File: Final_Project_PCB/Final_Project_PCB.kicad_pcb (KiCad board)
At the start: 2 copper layers, 90 x 93 mm, 17 parts, among them J1 Screw_Terminal_01x03, J2 SR04 Sensor Jarak, J3 LDR, J4 Soil Moisture Sensor, K1 SRD-05VDC-SL-C, Q1 BC547, U1 ESP32-DEVKIT-V1, U2 DHT11

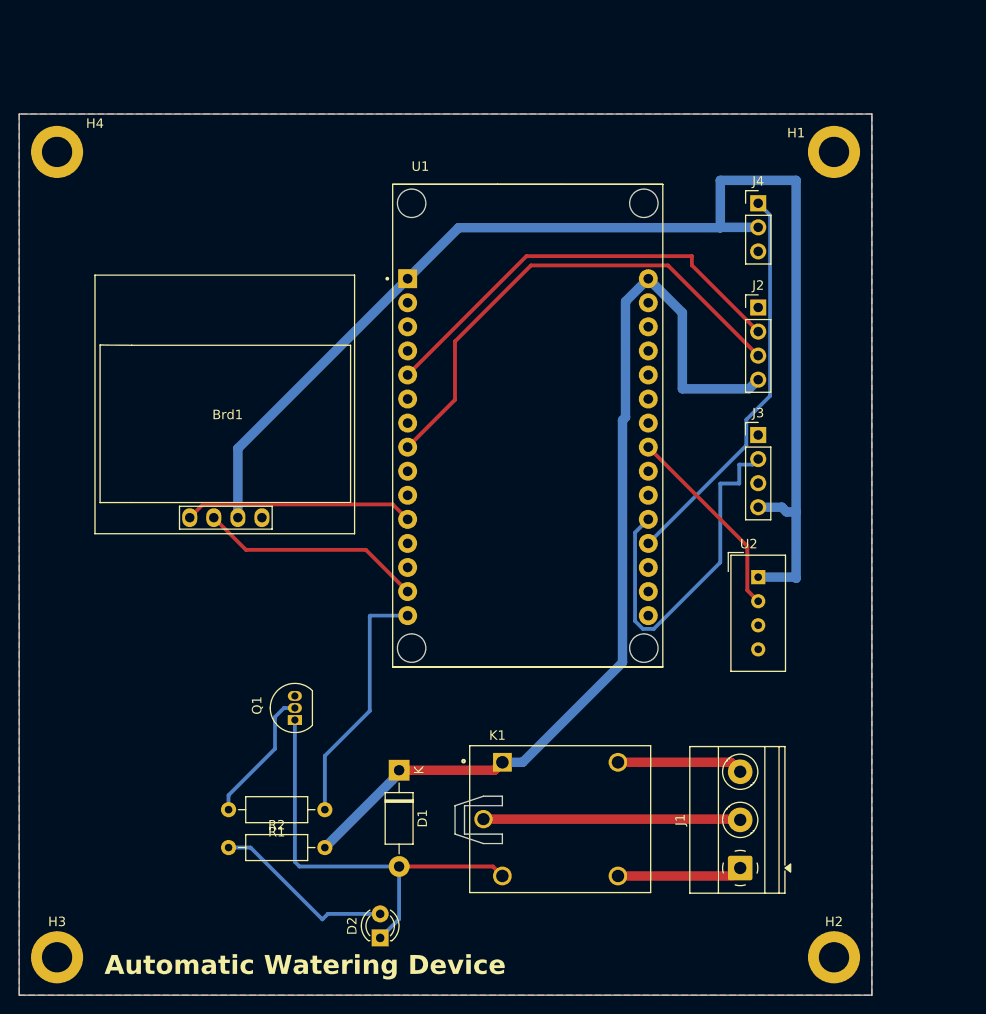
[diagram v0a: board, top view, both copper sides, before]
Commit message: Adding Barrel Jack for 5v Source
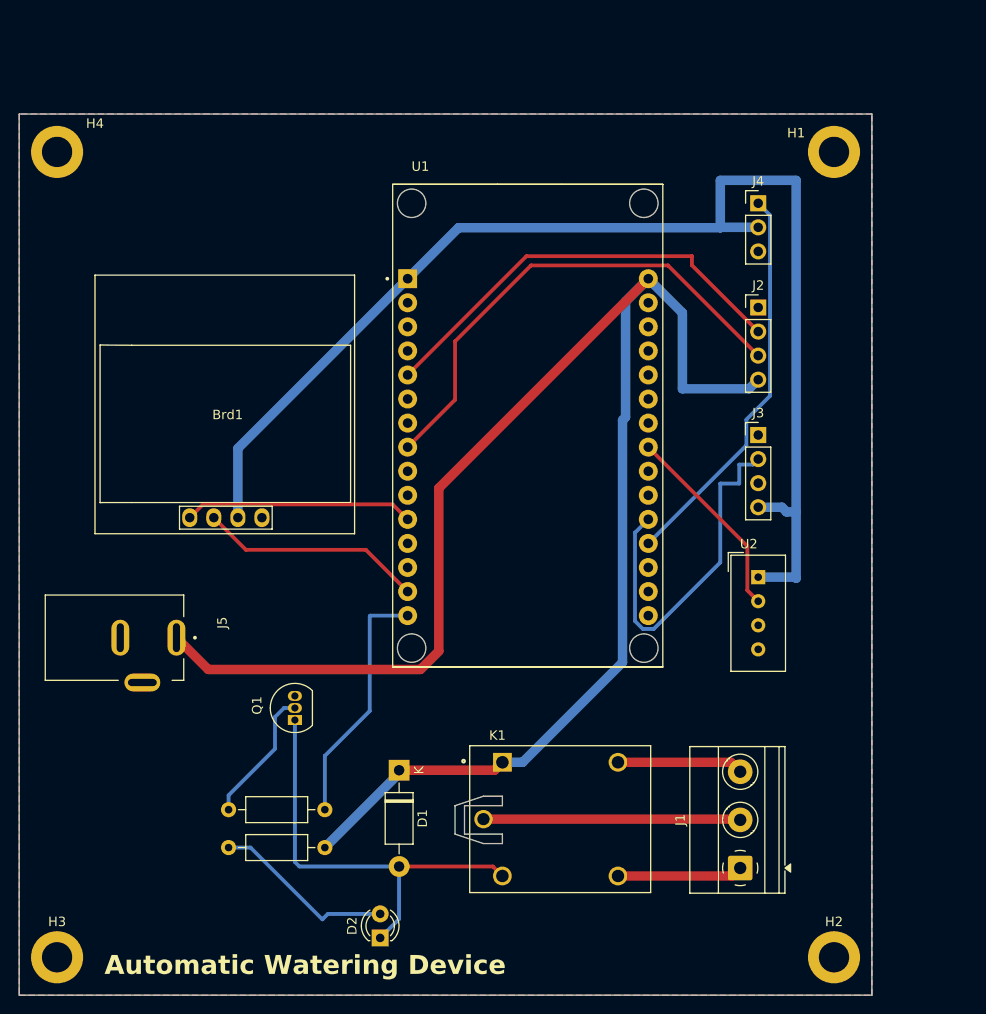
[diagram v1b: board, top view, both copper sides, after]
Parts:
- added J5: EJ503A, BARREL JACK 2.1MM KICAD:MPD_EJ503A, F.Cu at (160.1, 90.3)
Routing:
- net +5V: track 102.8 -> 181.2 mm

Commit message: Turn PCB to single layer and create a new gerber file
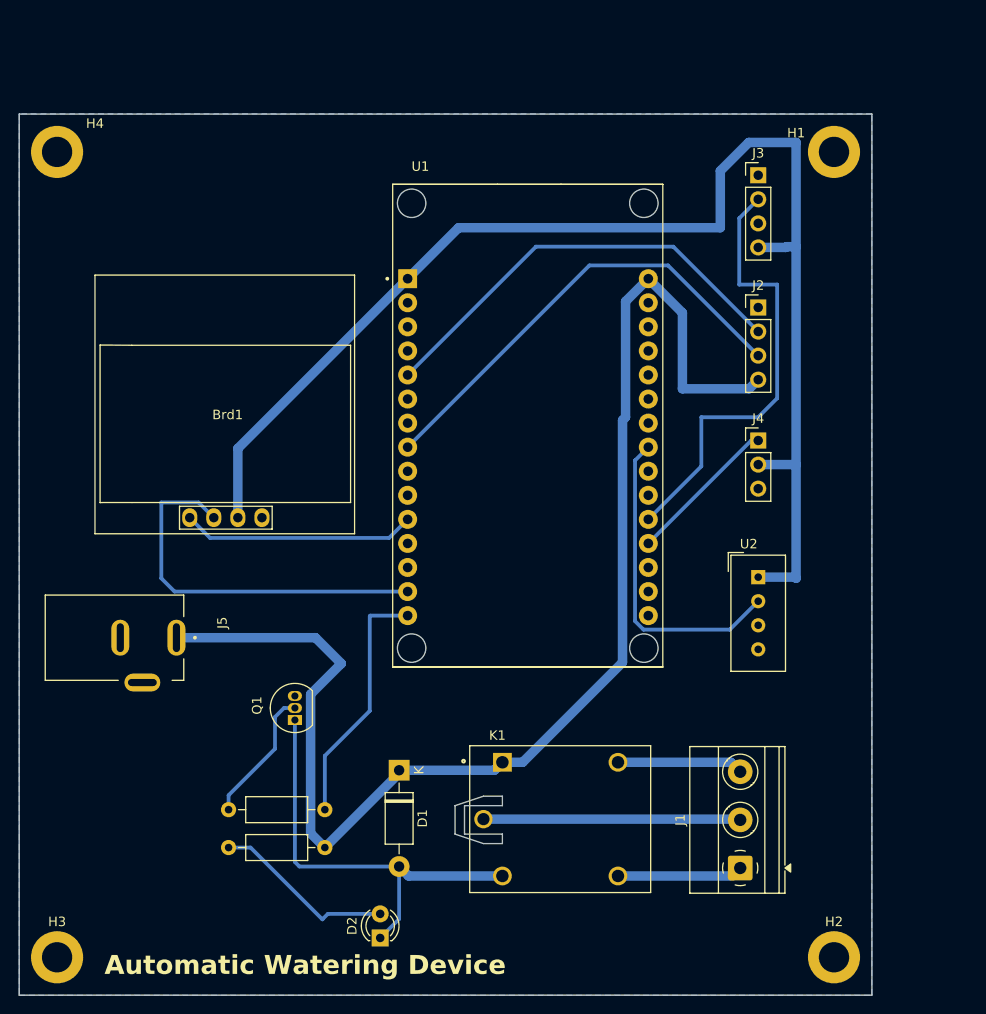
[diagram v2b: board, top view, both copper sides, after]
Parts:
- moved J3 27.4 mm to (228.0, 41.5)
- moved J4 25.0 mm to (228.0, 69.5)
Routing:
- net +5V: track 181.2 -> 142.8 mm
- net /AO_SOIL: track 41.7 -> 16.1 mm
- net /SCL: track 23.7 -> 40.8 mm
- net /DHT: track 21.1 -> 33.6 mm
- net /AO_LDR: track 38.1 -> 47.8 mm
- net +3.3V: track 135.1 -> 142.0 mm
- net /TRIG: track 52.5 -> 48.9 mm
- net Net-(J1-Pin_1): track 13.2 -> 14.4 mm
- removed copper zone on F.Cu, net GND

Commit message: Doing some revision on PCB and tidying up code
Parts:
- moved J3 30.9 mm to (234.0, 71.8)
- moved U2 27.5 mm to (234.0, 57.0)
- moved R1 23.1 mm to (191.0, 87.0)
- moved J4 18.6 mm to (234.0, 87.1)
- moved Q1 15.7 mm to (167.0, 108.9)
- moved J2 15.5 mm to (234.0, 41.1)
- moved H1 14.1 mm to (246.0, 29.0)
- moved H2 10.0 mm to (246.0, 124.0)
- moved H4 10.0 mm to (154.0, 29.0)
- moved Brd1 9.04 mm to (176.0, 58.9)
- moved J5 7.59 mm to (166.0, 95.0)
- moved D1 6.36 mm to (196.1, 102.2)
- moved J1 6.36 mm to (232.1, 112.5)
- moved K1 6.36 mm to (213.1, 107.3)
- moved R2 6.36 mm to (178.1, 110.3)
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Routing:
- net GND: track 0.00 -> 599.7 mm
- net +3.3V: track 142.0 -> 217.7 mm
- net /AO_LDR: track 47.8 -> 12.2 mm
- net Net-(Q1-B): track 14.3 -> 48.7 mm
- net /DHT: track 33.6 -> 12.9 mm
- net /RELAY: track 26.4 -> 6.44 mm
- net +5V: track 142.8 -> 161.9 mm
- net /SCL: track 40.8 -> 55.8 mm
- net Net-(D2-A): track 19.4 -> 8.07 mm
- net Net-(D1-A): track 45.9 -> 51.9 mm
- net /SDA: track 24.7 -> 30.4 mm
- net /TRIG: track 48.9 -> 46.1 mm
- net /ECHO: track 46.3 -> 44.0 mm
- net /AO_SOIL: track 16.1 -> 15.2 mm
- removed copper zone on B.Cu, net GND
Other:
- board size 90 x 93 mm -> 100 x 103 mm
